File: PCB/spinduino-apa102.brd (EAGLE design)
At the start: 78.5 x 86.8 mm, 27 parts

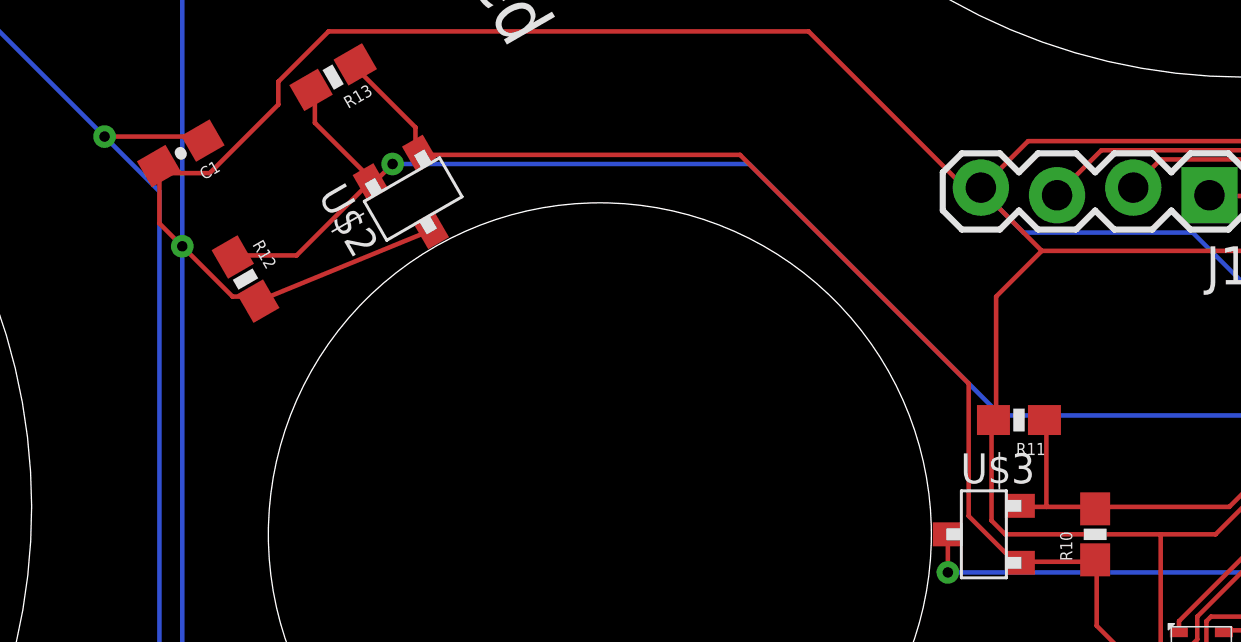
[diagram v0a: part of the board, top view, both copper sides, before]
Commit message: fix: remove redundant resistor
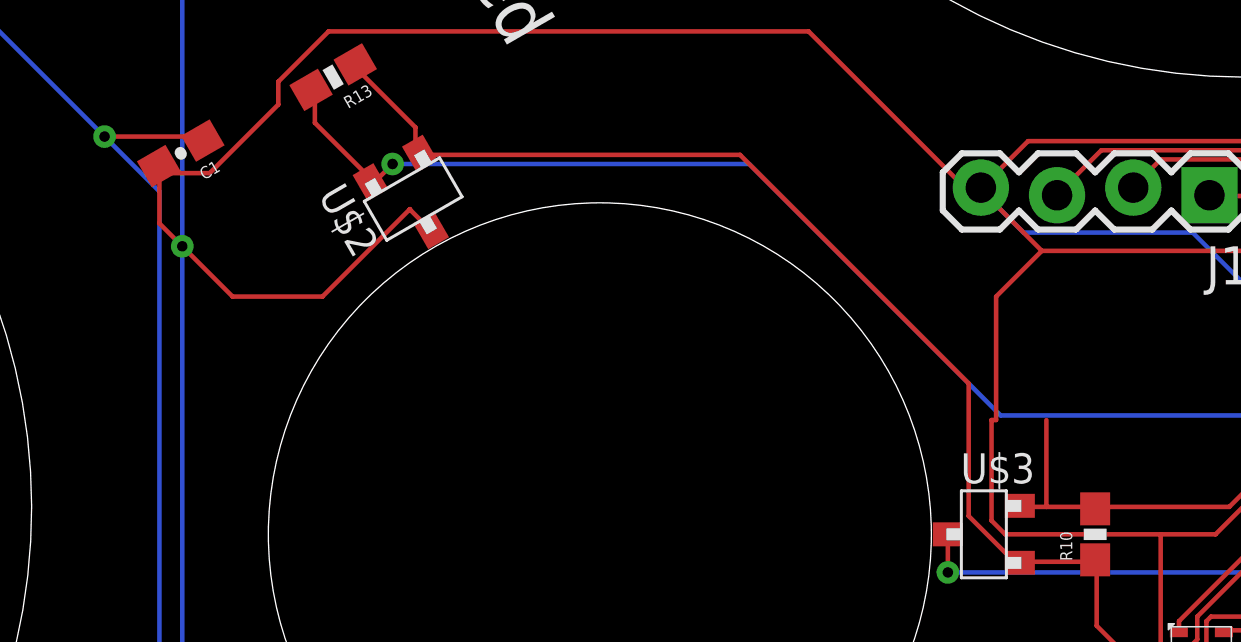
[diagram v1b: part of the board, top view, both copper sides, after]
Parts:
- removed R11, R12: 10K, SparkFun-Resistors:0603-RES
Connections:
- net GND: no longer R11.2, R12.2
- net HALL1: no longer R12.1
- net HALL2: no longer R11.1
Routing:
- net HALL1: track 52.3 -> 46.7 mm
- net GND: track 284.9 -> 285.8 mm
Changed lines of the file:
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@@
 <attribute name="PROD_ID" value="RES-00824" x="67.31" y="41.91" size="1.778" layer="27" rot="R90" display="off"/>
-</element>
-<element name="R11" library="SparkFun-Resistors" package="0603-RES" value="10K" x="64.77" y="45.72" rot="R180">
-<attribute name="PROD_ID" value="RES-00824" x="64.77" y="45.72" size="1.778" layer="27" rot="R180" display="off"/>
-</element>
-<element name="R12" library="SparkFun-Resistors" package="0603-RES" value="10K" x="38.989" y="50.419" rot="R300">
-<attribute name="PROD_ID" value="RES-00824" x="38.989" y="50.419" size="1.778" layer="27" rot="R300" display="off"/>
 </element>
 <element name="R13" library="SparkFun-Resistors" package="0603-RES" value="10K" x="41.91" y="57.15" rot="R210">
@@
 <contactref element="U$1" pad="25"/>
 <contactref element="U$1" pad="14"/>
-<contactref element="R11" pad="2"/>
 <contactref element="U$3" pad="3"/>
-<contactref element="R12" pad="2"/>
 <contactref element="C1" pad="2"/>
 <contactref element="C2" pad="2"/>
@@
 <wire x1="77.4192" y1="51.2064" x2="77.47" y2="51.22" width="0.1524" layer="1"/>
 <wire x1="74.9808" y1="51.2064" x2="74.93" y2="51.22" width="0.1524" layer="1"/>
-<wire x1="45.177" y1="52.04676875" x2="39.414" y2="49.682878125" width="0.1524" layer="1"/>
 <wire x1="91.8972" y1="44.6532" x2="91.8972" y2="44.3484" width="0.1524" layer="1"/>
 <wire x1="89.916" y1="46.6344" x2="91.8972" y2="44.6532" width="0.1524" layer="1"/>
@@
 <wire x1="63.8556" y1="45.72" x2="63.8556" y2="42.3672" width="0.1524" layer="1"/>
 <wire x1="82.1436" y1="44.3484" x2="82.28" y2="44.41" width="0.1524" layer="1"/>
-<wire x1="63.8556" y1="45.72" x2="63.92" y2="45.72" width="0.1524" layer="1"/>
 <wire x1="36.1188" y1="52.2732" x2="36.1188" y2="53.9496" width="0.1524" layer="1"/>
 <wire x1="36.1188" y1="53.9496" x2="36.1188" y2="54.102" width="0.1524" layer="1"/>
-<wire x1="38.5572" y1="49.8348" x2="36.8808" y2="51.5112" width="0.1524" layer="1"/>
+<wire x1="36.8808" y1="51.5112" x2="38.5572" y2="49.8348" width="0.1524" layer="1"/>
 <wire x1="36.8808" y1="51.5112" x2="36.1188" y2="52.2732" width="0.1524" layer="1"/>
-<wire x1="39.3192" y1="49.8348" x2="38.5572" y2="49.8348" width="0.1524" layer="1"/>
 <wire x1="36.1188" y1="54.102" x2="36.093878125" y2="54.185" width="0.1524" layer="1"/>
-<wire x1="39.3192" y1="49.8348" x2="39.414" y2="49.682878125" width="0.1524" layer="1"/>
 <wire x1="78.3336" y1="52.1208" x2="82.1436" y2="52.1208" width="0.1524" layer="1"/>
 <wire x1="77.5716" y1="51.3588" x2="78.3336" y2="52.1208" width="0.1524" layer="1"/>
@@
 <wire x1="64.008" y1="49.8348" x2="64.008" y2="45.72" width="0.1524" layer="1"/>
 <wire x1="65.532" y1="51.3588" x2="64.008" y2="49.8348" width="0.1524" layer="1"/>
-<wire x1="64.008" y1="45.72" x2="63.92" y2="45.72" width="0.1524" layer="1"/>
 <wire x1="80.6196" y1="41.91" x2="82.55" y2="41.91" width="0.1524" layer="16"/>
 <wire x1="79.341103125" y1="43.188496875" x2="70.5612" y2="51.9684" width="0.1524" layer="16"/>
@@
 <wire x1="92.0496" y1="39.1668" x2="93.5736" y2="39.1668" width="0.1524" layer="1"/>
 <wire x1="92.0496" y1="39.1668" x2="92.0136" y2="39.1724" width="0.1524" layer="1"/>
+<wire x1="44.46155" y1="52.74321875" x2="41.55313125" y2="49.8348" width="0.1524" layer="1"/>
+<wire x1="44.46155" y1="52.74321875" x2="44.47105" y2="52.75271875" width="0.1524" layer="1"/>
+<wire x1="38.5572" y1="49.8348" x2="41.55313125" y2="49.8348" width="0.1524" layer="1"/>
+<wire x1="45.177" y1="52.04676875" x2="45.158" y2="52.04676875" width="0.1524" layer="1"/>
+<wire x1="45.158" y1="52.04676875" x2="44.46155" y2="52.74321875" width="0.1524" layer="1"/>
+<wire x1="64.008" y1="45.72" x2="63.8556" y2="45.72" width="0.1524" layer="1"/>
 </signal>
 <signal name="HALL1">
 <contactref element="U$1" pad="23"/>
 <contactref element="U$2" pad="2"/>
-<contactref element="R12" pad="1"/>
 <contactref element="R13" pad="2"/>
-<wire x1="40.6908" y1="51.2064" x2="38.7096" y2="51.2064" width="0.1524" layer="1"/>
-<wire x1="43.1292" y1="53.6448" x2="40.6908" y2="51.2064" width="0.1524" layer="1"/>
-<wire x1="38.7096" y1="51.2064" x2="38.564" y2="51.15511875" width="0.1524" layer="1"/>
 <wire x1="43.1292" y1="53.6448" x2="43.154275" y2="53.650228125" width="0.1524" layer="1"/>
 <wire x1="41.3004" y1="55.626" x2="41.3004" y2="56.6928" width="0.1524" layer="1"/>
@@
 <contactref element="U$3" pad="2"/>
 <contactref element="R10" pad="2"/>
-<contactref element="R11" pad="1"/>
 <wire x1="67.2084" y1="42.8244" x2="65.6844" y2="42.8244" width="0.1524" layer="1"/>
 <wire x1="65.6844" y1="42.8244" x2="64.77" y2="42.8244" width="0.1524" layer="1"/>
@@
 <wire x1="67.2084" y1="42.8244" x2="67.31" y2="42.76" width="0.1524" layer="1"/>
 <wire x1="65.6844" y1="42.8244" x2="65.6844" y2="45.72" width="0.1524" layer="1"/>
-<wire x1="65.6844" y1="45.72" x2="65.62" y2="45.72" width="0.1524" layer="1"/>
 <wire x1="75.438" y1="46.482" x2="80.772" y2="46.482" width="0.1524" layer="1"/>
 <wire x1="71.7804" y1="42.8244" x2="75.438" y2="46.482" width="0.1524" layer="1"/>

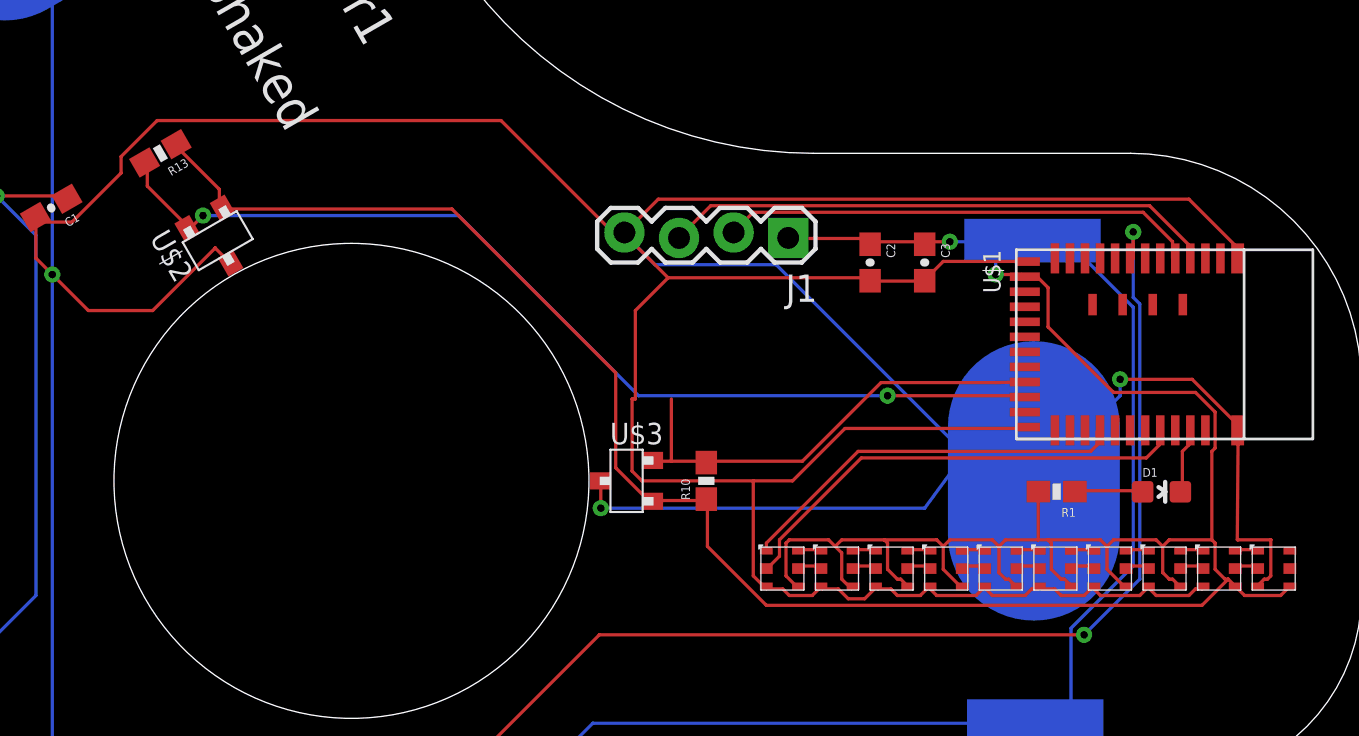
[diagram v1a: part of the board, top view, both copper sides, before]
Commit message: Make hall effect sensors powered by CPU
This will help with standby power consumption
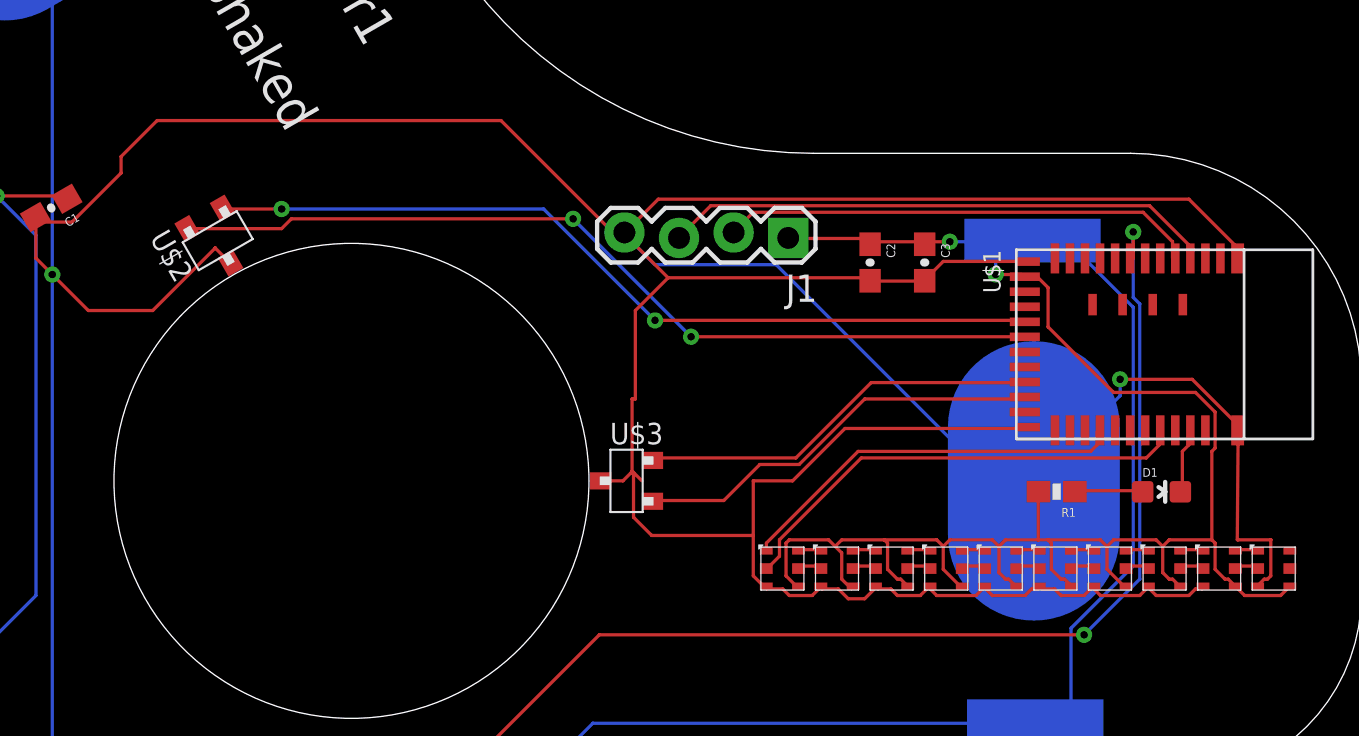
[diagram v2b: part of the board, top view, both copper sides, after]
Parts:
- removed R10, R13: 10K, SparkFun-Resistors:0603-RES
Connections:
- new net HALL1PWR: U$1.18, U$2.1
- new net HALL2PWR: U$1.23, U$3.1
- net HALL1: now also U$1.19; no longer R13.2, U$1.23
- net HALL2: no longer R10.2
- net V_BATT: no longer R10.1, R13.1, U$2.1, U$3.1
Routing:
- net V_BATT: track 327.2 -> 264.2 mm
- net HALL1PWR: track 0.00 -> 39.5 mm, vias 0 -> 2
- net HALL2PWR: track 0.00 -> 19.7 mm
- net GND: track 285.8 -> 271.0 mm, vias 4 -> 3
- net HALL1: track 46.7 -> 41.5 mm
- net HALL2: track 21.9 -> 18.9 mm
